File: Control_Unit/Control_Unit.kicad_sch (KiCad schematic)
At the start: 0 parts

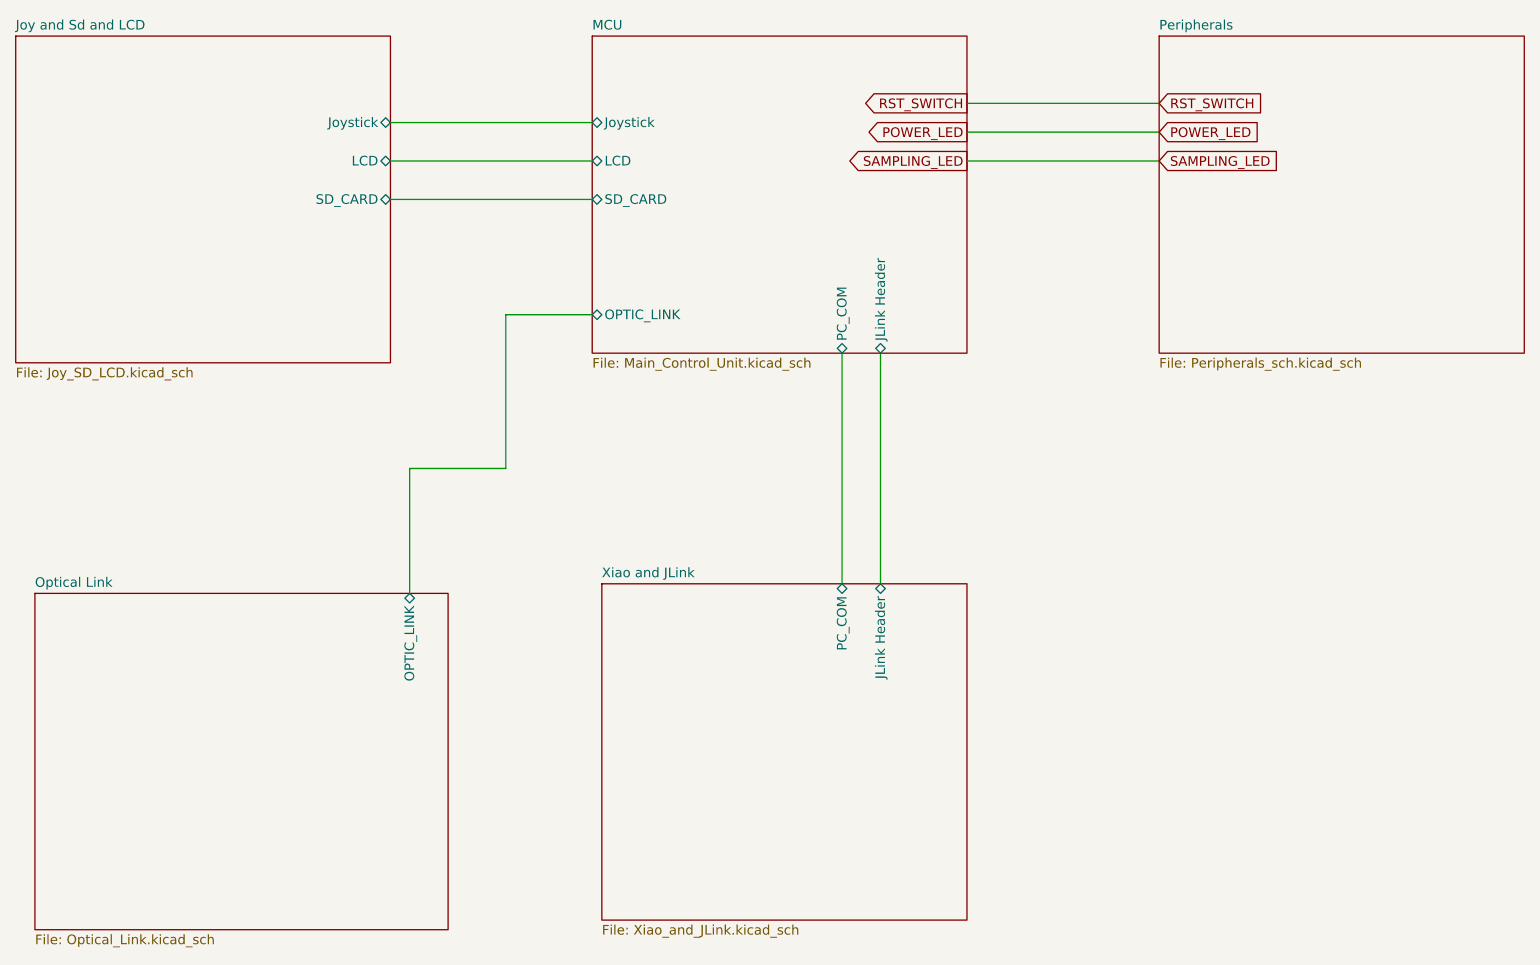
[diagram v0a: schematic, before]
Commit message: Control Unit Schematics and PCB.
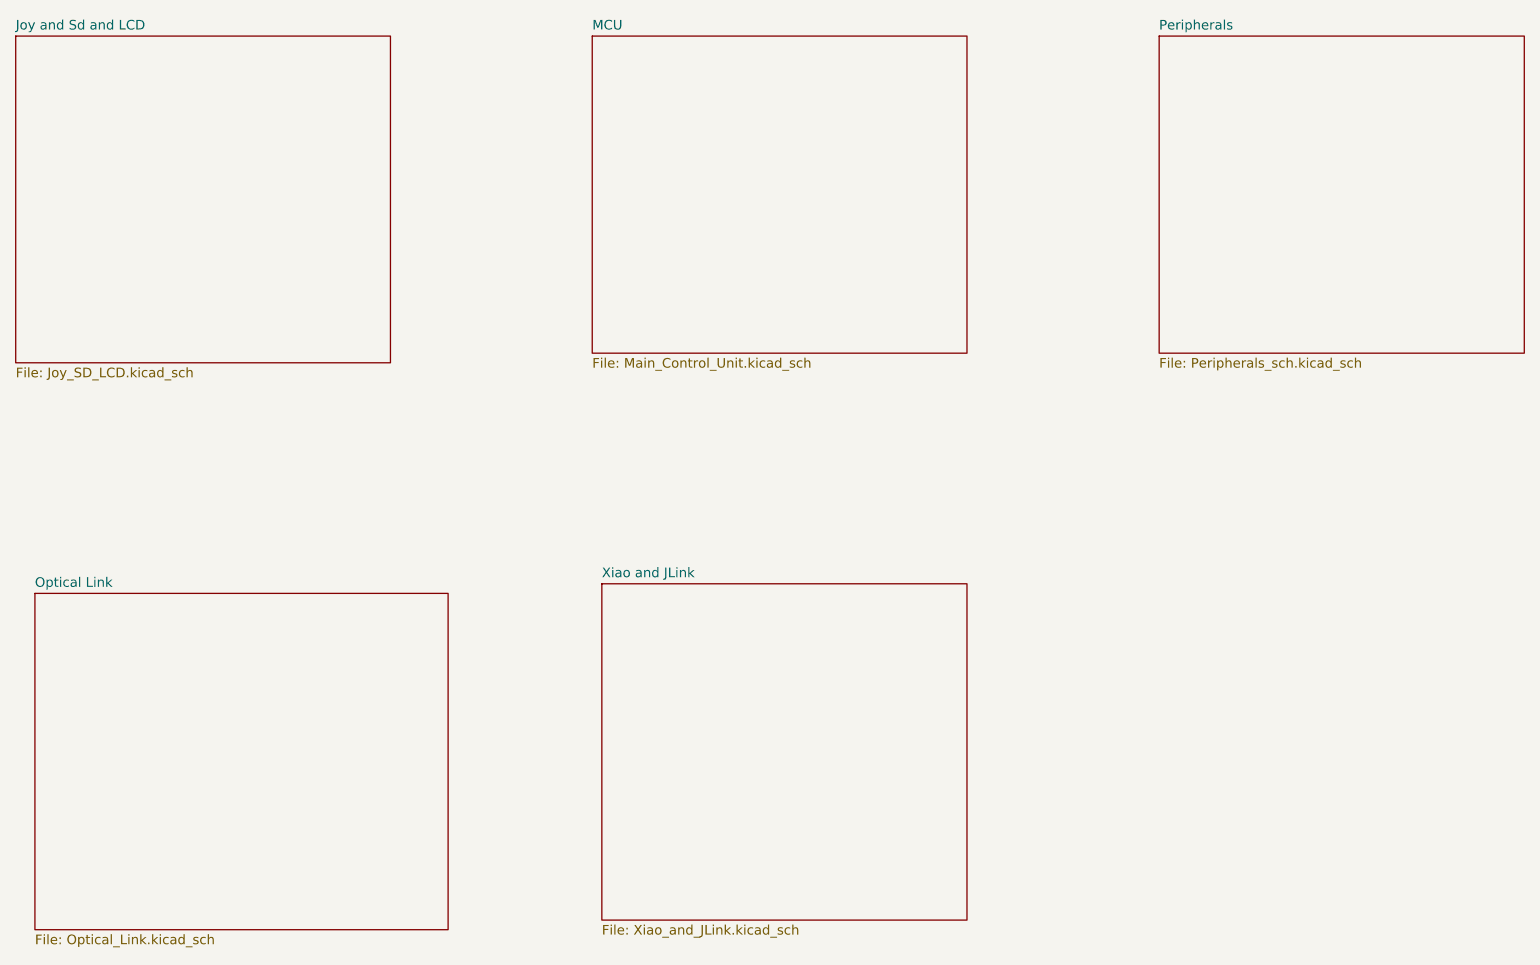
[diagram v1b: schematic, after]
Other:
- sheet Joy and Sd and LCD ports: added none; removed Joystick, LCD, SD_CARD
- sheet MCU ports: added none; removed JLink Header, Joystick, LCD, OPTIC_LINK, PC_COM, SD_CARD
- sheet Optical Link ports: added none; removed OPTIC_LINK
- sheet Xiao and JLink ports: added none; removed JLink Header, PC_COM
